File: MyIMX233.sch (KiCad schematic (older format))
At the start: 71 parts, among them IC1 iMX233, IC2 DDR_SDRAM_MT46_x16, J1 USB_A, J2 Micro_SD_Card, P1 P4v2, P2 1v2, P3 VDDA1v8, P4 2v5, P5 3v3, SW1 SWITCH_PUSHBUTTON, Y1 24Mhz

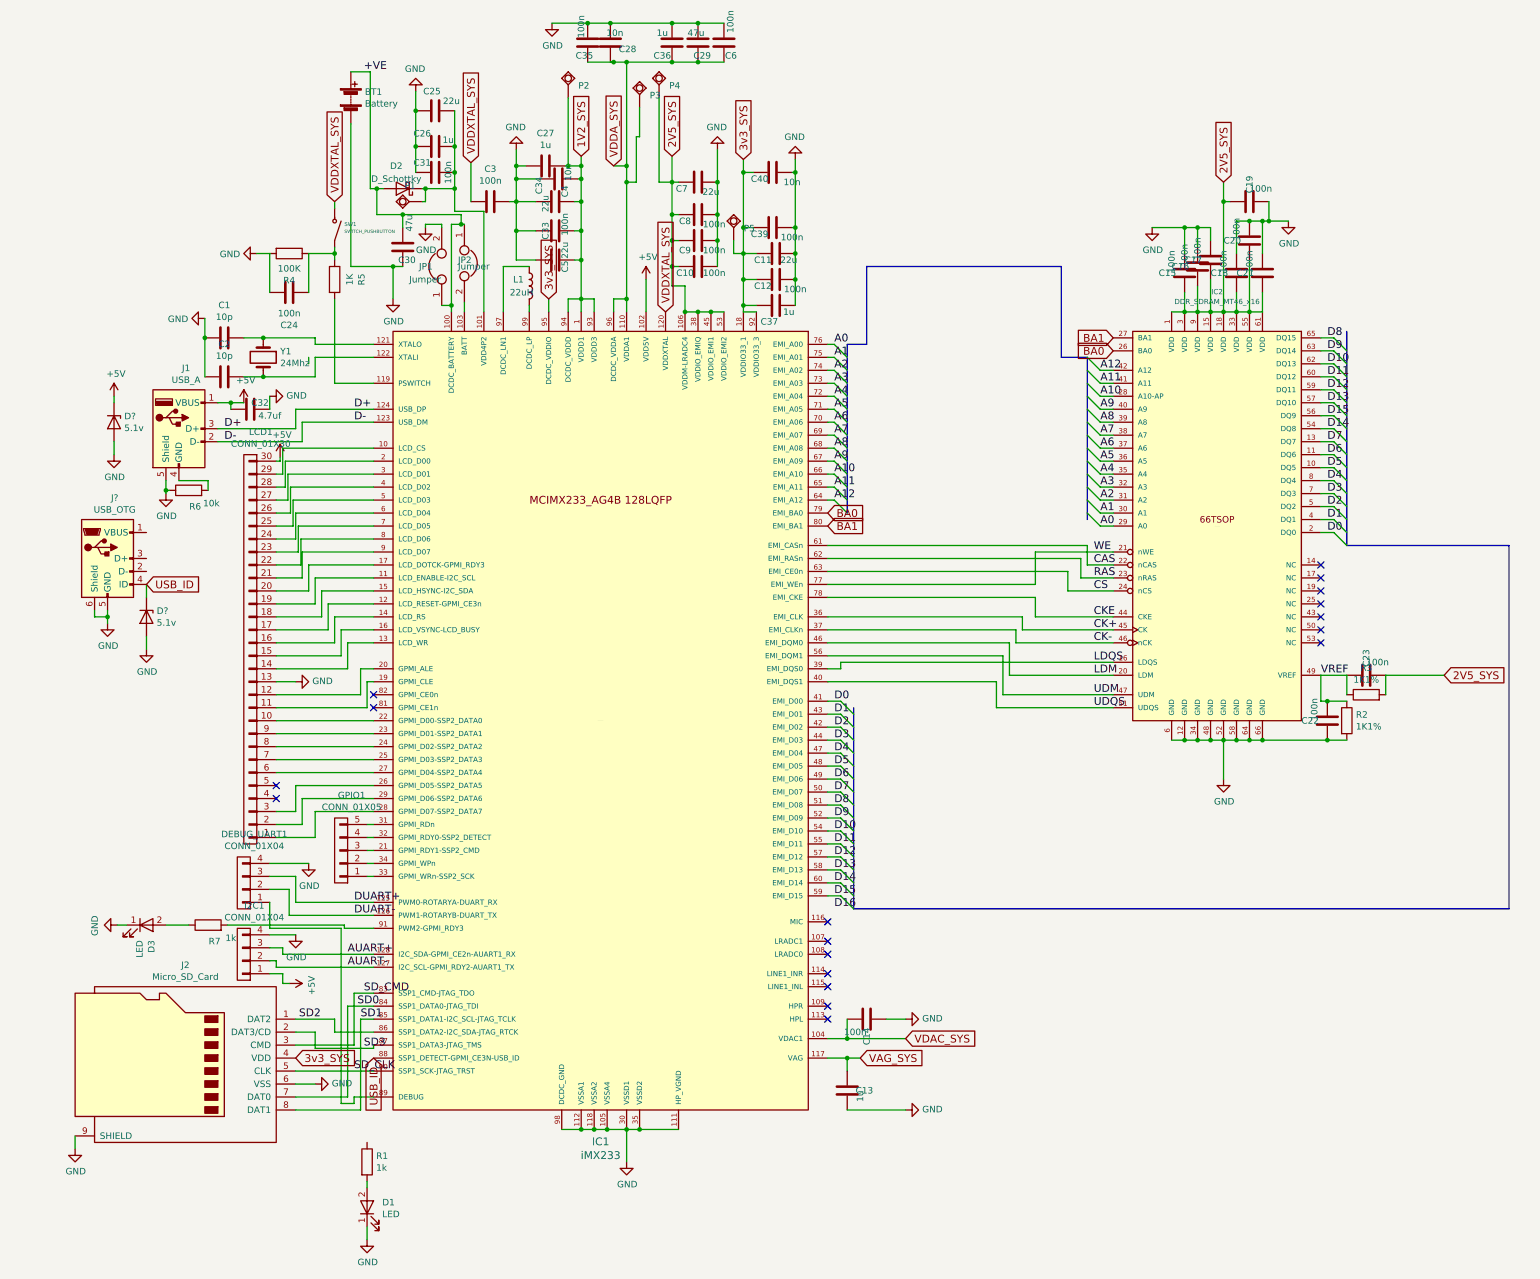
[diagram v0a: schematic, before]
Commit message: new uSD card connector added
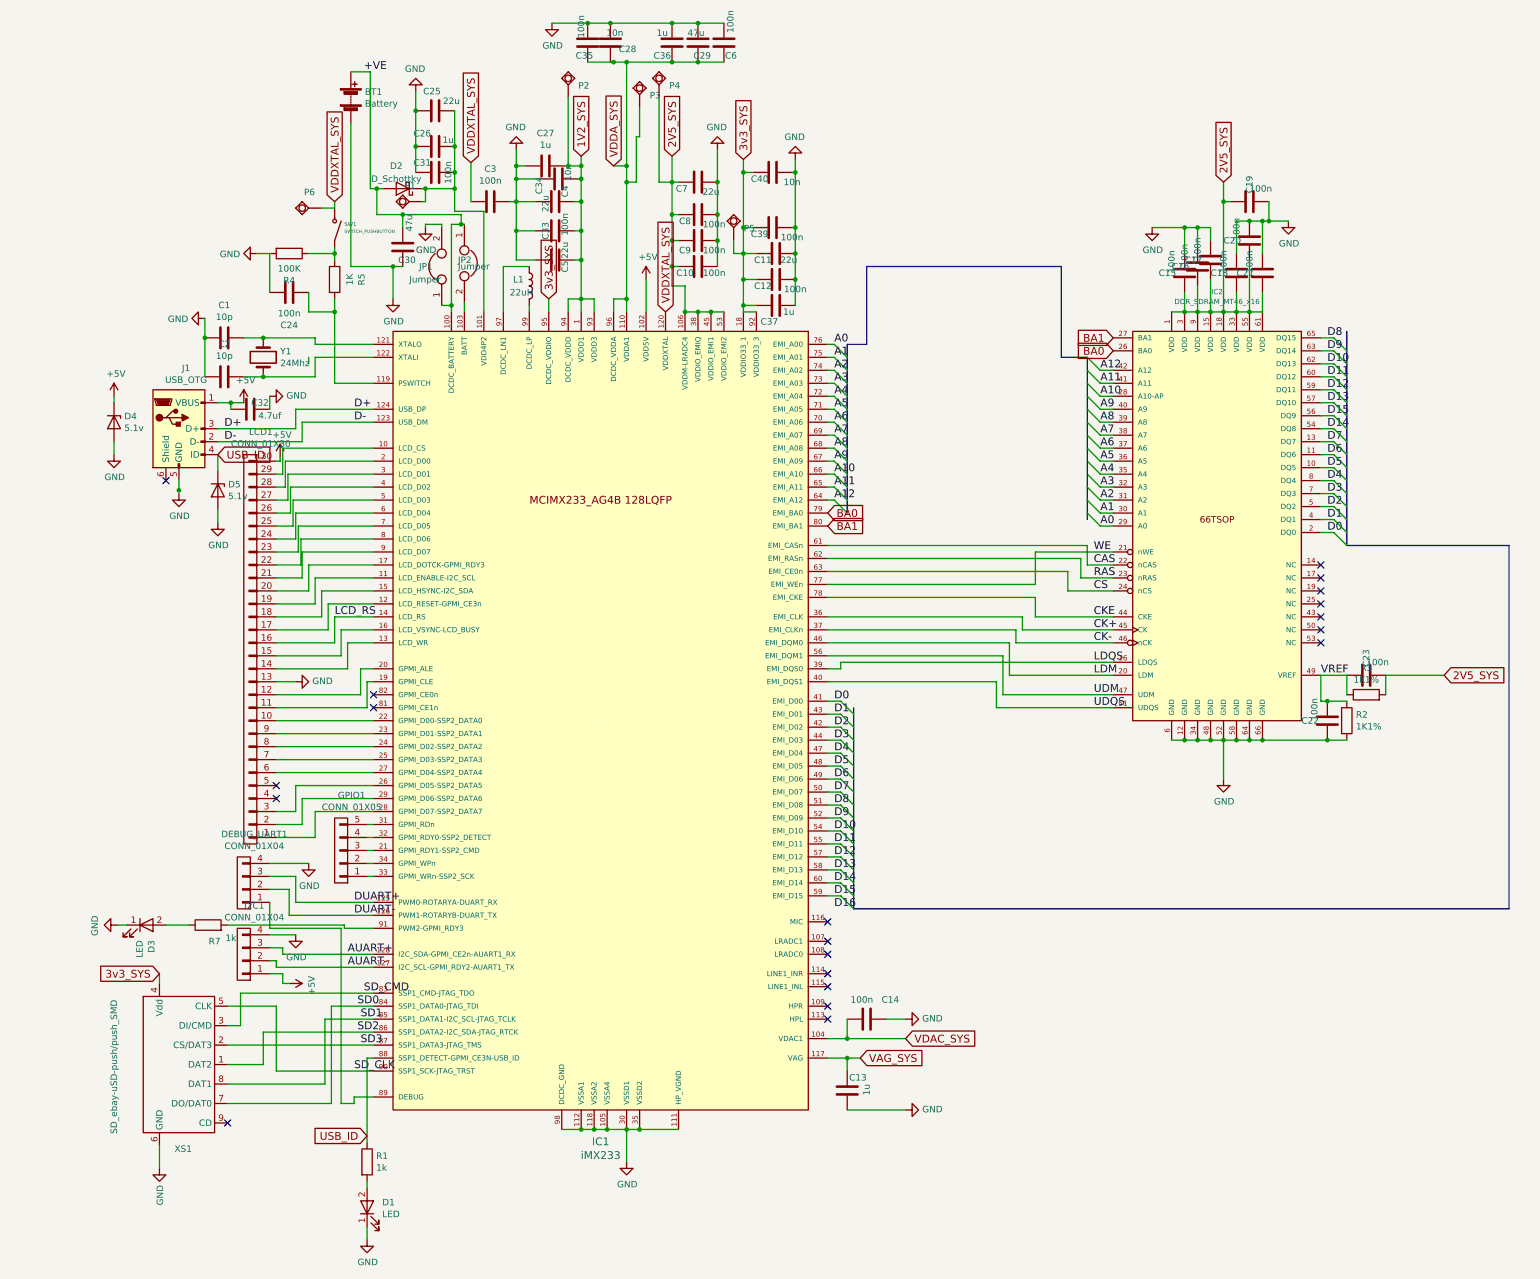
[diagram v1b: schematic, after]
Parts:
- removed J1: USB_A, conn-fci:CONN-10118194-0001LF-FCI, symbol USB_A
- removed J2: Micro_SD_Card, mylib:microSD_Card_Receptacle_Hirose_DM3AT-SF-PEJM5, symbol Micro_SD_Card
- removed J?: USB_OTG, symbol USB_OTG
- removed R6: 10k, Resistors_SMD:R_0603_HandSoldering, symbol R
- added J1: USB_OTG, mylib:CONN-10118194-0001LF-FCI, symbol USB_OTG
- added P6: P4v2, iMX233-OLinuXino-NANO_Rev_BEagle:GOGO_TESTPAD2, symbol GOGO_TESTPAD
- added XS1: SD_ebay-uSD-push/push_SMD, mylib:uSDcard, symbol SD_ebay-uSD-push/push_SMD
- D4, D5: renamed from D?; footprint (none) -> Diodes_SMD:D_SOD-323_HandSoldering
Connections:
- net +5V: now also J1.1 (VBUS)
- net 3v3_SYS: now also XS1.4 (Vdd)
- net D+: now also J1.3 (D+)
- net D-: now also J1.2 (D-)
- net GND: now also XS1.6 (GND)
- net SD0: now also XS1.7 (DO/DAT0)
- net SD1: now also XS1.8 (DAT1)
- net SD2: now also XS1.1 (DAT2)
- net SD3: now also XS1.2 (CS/DAT3)
- net SD_CLK: now also XS1.5 (CLK)
- net SD_CMD: now also XS1.3 (DI/CMD)
- net USB_ID: now also R1.1, J1.4 (ID)
- net VDDXTAL_SYS: now also P6.P$1 (PP)
- net at IC1.119 (PSWITCH), R5.2: now also C24.2
- net LCD_RS: now reaches IC1.14 (LCD_RS), LCD1.16 (P16)
- net at R4.1, R5.1, SW1.2 (B): no longer C24.2
- no-connect marks 18 -> 20
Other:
- moved on the sheet: D5

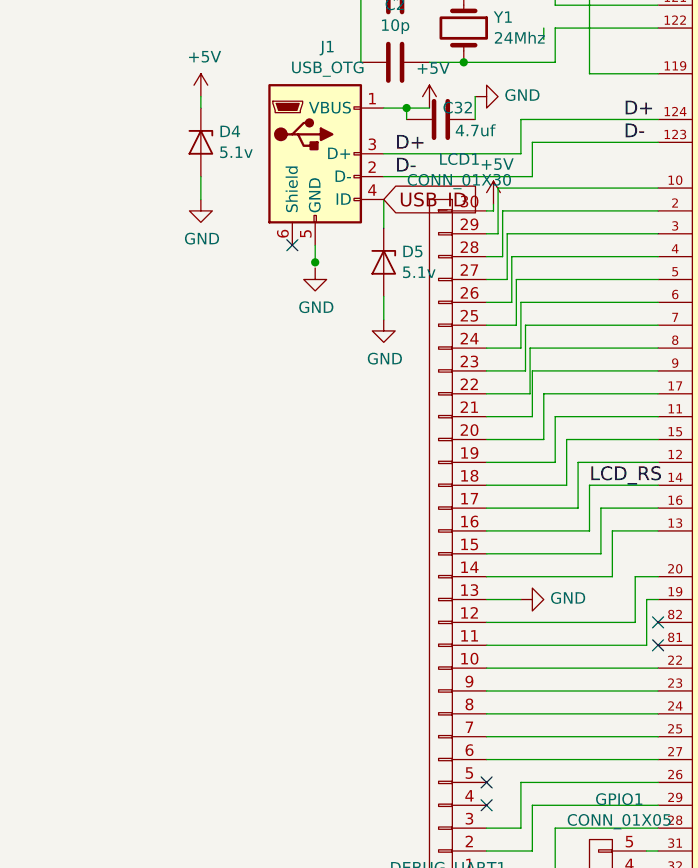
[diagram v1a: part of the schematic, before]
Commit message: usb footprint updated
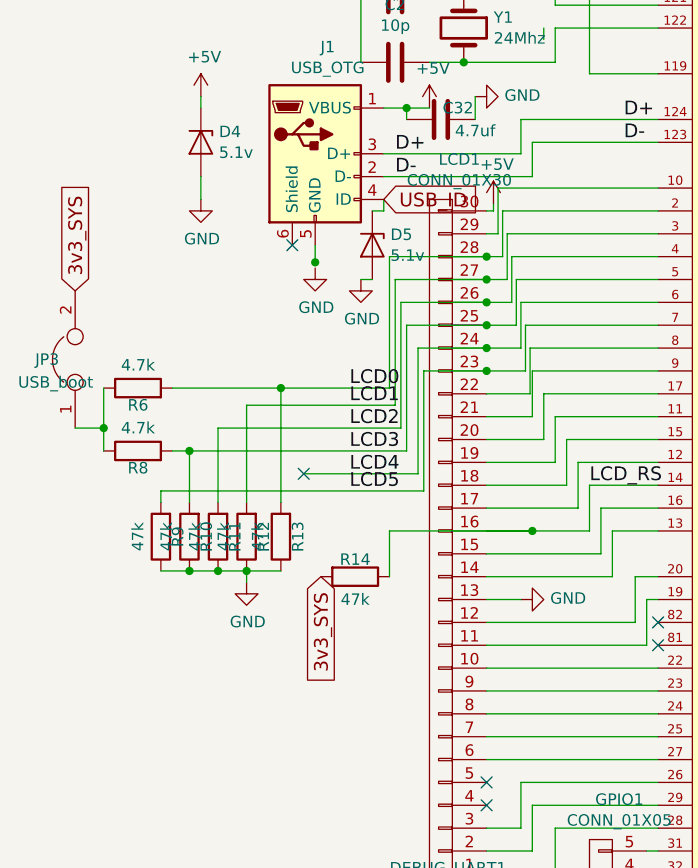
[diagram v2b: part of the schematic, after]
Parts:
- added JP3: USB_boot, Pin_Headers:Pin_Header_Straight_1x02_Pitch2.54mm, symbol Jumper
- added R10, R11, R12, R13, R14, R9: 47k, Resistors_SMD:R_0603_HandSoldering, symbol R
- added R6, R8: 4.7k, Resistors_SMD:R_0603_HandSoldering, symbol R
- J1: footprint mylib:CONN-10118194-0001LF-FCI -> mylib:USB_Micro-B_MOLEX_105017-0001
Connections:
- net 3v3_SYS: now also JP3.2, R14.2
- net GND: now also R10.1, R11.1, R12.1, R13.1, R9.1
- net LCD_RS: now also R14.1
- net LCD0: now reaches IC1.2 (LCD_D00), LCD1.28 (P28)
- net LCD0: now also R13.2, R6.2
- net LCD1: now reaches IC1.3 (LCD_D01), LCD1.27 (P27)
- net LCD1: now also R12.2
- net LCD2: now reaches IC1.4 (LCD_D02), LCD1.26 (P26)
- net LCD2: now also R11.2
- net LCD3: now reaches IC1.5 (LCD_D03), LCD1.25 (P25)
- net LCD3: now also R10.2, R8.2
- net LCD4: now reaches IC1.6 (LCD_D04), LCD1.24 (P24)
- net LCD5: now reaches IC1.7 (LCD_D05), LCD1.23 (P23)
- net LCD5: now also R9.2
- new net: JP3.1, R6.1, R8.1
- no-connect marks 20 -> 21
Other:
- moved on the sheet: D5
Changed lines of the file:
@@
 	2690 4500 3250 4500
 Wire Wire Line
-	2500 4600 2670 4600
+	2225 4600 2670 4600
 Wire Wire Line
 	2670 4600 2670 4400
@@
 	2670 4400 3250 4400
 Wire Wire Line
-	2500 4500 2650 4500
-Wire Wire Line
 	2650 4500 2650 4300
 Wire Wire Line
 	2650 4300 3250 4300
 Wire Wire Line
-	2500 4400 2630 4400
+	2150 4400 2630 4400
 Wire Wire Line
 	2630 4400 2630 4200
@@
 	2630 4200 3250 4200
 Wire Wire Line
-	2500 4300 2610 4300
+	2125 4300 2610 4300
 Wire Wire Line
 	2610 4300 2610 4100
@@
 	2610 4100 3250 4100
 Wire Wire Line
-	2500 4200 2590 4200
+	2100 4200 2590 4200
 Wire Wire Line
 	2590 4200 2590 4000
@@
 	2590 4000 3250 4000
 Wire Wire Line
-	2500 4100 2570 4100
+	2075 4100 2570 4100
 Wire Wire Line
 	2570 4100 2570 3900
@@
 L D_Zener D5
 U 1 1 598BC40A
-P 2050 4125
-F 0 "D5" V 2004 4204 50  0000 L CNN
-F 1 "5.1v" V 2095 4204 50  0000 L CNN
-F 2 "Diodes_SMD:D_SOD-323_HandSoldering" H 2050 4125 50  0001 C CNN
-F 3 "" H 2050 4125 50  0001 C CNN
-	1    2050 4125
+P 2000 4050
+F 0 "D5" V 1954 4129 50  0000 L CNN
+F 1 "5.1v" V 2045 4129 50  0000 L CNN
+F 2 "Diodes_SMD:D_SOD-323_HandSoldering" H 2000 4050 50  0001 C CNN
+F 3 "" H 2000 4050 50  0001 C CNN
+	1    2000 4050
 	0    1    1    0
 $EndComp
@@
 L GND #PWR030
 U 1 1 598BC5E8
-P 2050 4375
-F 0 "#PWR030" H 2050 4125 50  0001 C CNN
-F 1 "GND" H 2055 4202 50  0000 C CNN
-F 2 "" H 2050 4375 50  0001 C CNN
-F 3 "" H 2050 4375 50  0001 C CNN
-	1    2050 4375
+P 1950 4200
+F 0 "#PWR030" H 1950 3950 50  0001 C CNN
+F 1 "GND" H 1955 4027 50  0000 C CNN
+F 2 "" H 1950 4200 50  0001 C CNN
+F 3 "" H 1950 4200 50  0001 C CNN
+	1    1950 4200
 	1    0    0    -1
 $EndComp
@@
 F 0 "J1" H 1805 4117 50  0000 C CNN
 F 1 "USB_OTG" H 1805 4026 50  0000 C CNN
-F 2 "mylib:CONN-10118194-0001LF-FCI" H 1900 3600 50  0001 C CNN
+F 2 "mylib:USB_Micro-B_MOLEX_105017-0001" H 1900 3600 50  0001 C CNN
 F 3 "" H 1900 3600 50  0001 C CNN
 	1    1750 3650
@@
 $EndComp
 Wire Wire Line
-	2050 3975 2050 3850
-Wire Wire Line
 	1750 4125 1750 4050
 Connection ~ 1750 4125
-Wire Wire Line
-	2050 4275 2050 4375
 NoConn ~ 1650 4050
+$Comp
+L R R14
+U 1 1 5992DA70
+P 1925 5500
+F 0 "R14" V 1850 5500 50  0000 C CNN
+F 1 "47k" V 2025 5500 50  0000 C CNN
+F 2 "Resistors_SMD:R_0603_HandSoldering" V 1855 5500 50  0001 C CNN
+F 3 "" H 1925 5500 50  0001 C CNN
+	1    1925 5500
+	0    1    1    0
+$EndComp
+Connection ~ 2700 5300
+Text GLabel 700  4250 1    60   Input ~ 0
+3v3_SYS
+Connection ~ 2500 4100
+Connection ~ 2500 4200
+Connection ~ 2500 4300
+Connection ~ 2500 4400
+Wire Wire Line
+	1700 5050 2200 5050
+Connection ~ 2500 4500
+Connection ~ 2500 4600
+Wire Wire Line
+	2050 3900 2050 3850
+Wire Wire Line
+	1950 4200 2000 4200
+Wire Wire Line
+	2000 3900 2050 3900
+Wire Wire Line
+	2075 4675 2075 4100
+Wire Wire Line
+	1125 4675 2075 4675
+Wire Wire Line
+	2100 4750 2100 4200
+Wire Wire Line
+	2125 4850 2125 4300
+Wire Wire Line
+	2200 4500 2650 4500
+Wire Wire Line
+	2200 5050 2200 4500
+Wire Wire Line
+	2150 4950 2150 4400
+Wire Wire Line
+	1125 4950 2150 4950
+Wire Wire Line
+	2225 5125 2225 4600
+Wire Wire Line
+	1075 5125 2225 5125
+Text Label 1900 5125 0    60   ~ 0
+LCD5
+Text Label 1900 5050 0    60   ~ 0
+LCD4
+Text Label 1900 4950 0    60   ~ 0
+LCD3
+Text Label 1900 4850 0    60   ~ 0
+LCD2
+Text Label 1900 4750 0    60   ~ 0
+LCD1
+Text Label 1900 4675 0    60   ~ 0
+LCD0
+$Comp
+L R R13
+U 1 1 59940018
+P 1600 5325
+F 0 "R13" V 1525 5325 50  0000 C CNN
+F 1 "47k" V 1700 5325 50  0000 C CNN
+F 2 "Resistors_SMD:R_0603_HandSoldering" V 1530 5325 50  0001 C CNN
+F 3 "" H 1600 5325 50  0001 C CNN
+	1    1600 5325
+	-1   0    0    1
+$EndComp
+$Comp
+L GND #PWR031
+U 1 1 599401F2
+P 1450 5525
+F 0 "#PWR031" H 1450 5275 50  0001 C CNN
+F 1 "GND" H 1455 5352 50  0000 C CNN
+F 2 "" H 1450 5525 50  0001 C CNN
+F 3 "" H 1450 5525 50  0001 C CNN
+	1    1450 5525
+	1    0    0    -1
+$EndComp
+$Comp
+L R R12
+U 1 1 59941454
+P 1450 5325
+F 0 "R12" V 1375 5325 50  0000 C CNN
+F 1 "47k" V 1550 5325 50  0000 C CNN
+F 2 "Resistors_SMD:R_0603_HandSoldering" V 1380 5325 50  0001 C CNN
+F 3 "" H 1450 5325 50  0001 C CNN
+	1    1450 5325
+	-1   0    0    1
+$EndComp
+$Comp
+L R R11
+U 1 1 5994150A
+P 1325 5325
+F 0 "R11" V 1250 5325 50  0000 C CNN
+F 1 "47k" V 1425 5325 50  0000 C CNN
+F 2 "Resistors_SMD:R_0603_HandSoldering" V 1255 5325 50  0001 C CNN
+F 3 "" H 1325 5325 50  0001 C CNN
+	1    1325 5325
+	-1   0    0    1
+$EndComp
+$Comp
+L R R10
+U 1 1 599415B8
+P 1200 5325
+F 0 "R10" V 1125 5325 50  0000 C CNN
+F 1 "47k" V 1300 5325 50  0000 C CNN
+F 2 "Resistors_SMD:R_0603_HandSoldering" V 1130 5325 50  0001 C CNN
+F 3 "" H 1200 5325 50  0001 C CNN
+	1    1200 5325
+	-1   0    0    1
+$EndComp
+NoConn ~ 1700 5050
+Wire Wire Line
+	1600 5175 1600 4675
+Connection ~ 1600 4675
+Wire Wire Line
+	1450 5175 1450 4750
+Wire Wire Line
+	1325 5175 1325 4850
+Wire Wire Line
+	1325 4850 2125 4850
+Wire Wire Line
+	1200 5175 1200 4950
+Connection ~ 1200 4950
+$Comp
+L R R9
+U 1 1 59942CD2
+P 1075 5325
+F 0 "R9" V 1000 5325 50  0000 C CNN
+F 1 "47k" V 1175 5325 50  0000 C CNN
+F 2 "Resistors_SMD:R_0603_HandSoldering" V 1005 5325 50  0001 C CNN
+F 3 "" H 1075 5325 50  0001 C CNN
+	1    1075 5325
+	-1   0    0    1
+$EndComp
+Wire Wire Line
+	1075 5175 1075 5125
+Wire Wire Line
+	1075 5475 1600 5475
+Connection ~ 1200 5475
+Connection ~ 1325 5475
+Connection ~ 1450 5475
+Wire Wire Line
+	1450 5525 1450 5475
+Wire Wire Line
+	2075 5500 2075 5300
+Wire Wire Line
+	2075 5300 2700 5300
+$Comp
+L R R6
+U 1 1 599451CF
+P 975 4675
+F 0 "R6" V 900 4675 50  0000 C CNN
+F 1 "4.7k" V 1075 4675 50  0000 C CNN
+F 2 "Resistors_SMD:R_0603_HandSoldering" V 905 4675 50  0001 C CNN
+F 3 "" H 975 4675 50  0001 C CNN
+	1    975  4675
+	0    -1   -1   0
+$EndComp
+$Comp
+L R R8
+U 1 1 5994533A
+P 975 4950
+F 0 "R8" V 900 4950 50  0000 C CNN
+F 1 "4.7k" V 1075 4950 50  0000 C CNN
+F 2 "Resistors_SMD:R_0603_HandSoldering" V 905 4950 50  0001 C CNN
+F 3 "" H 975 4950 50  0001 C CNN
+	1    975  4950
+	0    -1   -1   0
+$EndComp
+Wire Wire Line
+	825  4950 825  4675
+Text GLabel 1775 5500 3    60   Input ~ 0
+3v3_SYS
+Wire Wire Line
+	1450 4750 2100 4750
+$Comp
+L Jumper JP3
+U 1 1 59949205
+P 700 4550
+F 0 "JP3" V 700 4725 50  0000 R CNN
+F 1 "USB_boot" V 600 4800 50  0000 R CNN
+F 2 "Pin_Headers:Pin_Header_Straight_1x02_Pitch2.54mm" H 700 4550 50  0001 C CNN
+F 3 "" H 700 4550 50  0001 C CNN
+	1    700  4550
+	0    -1   -1   0
+$EndComp
+Wire Wire Line
+	700  4850 825  4850
+Connection ~ 825  4850
 $EndSCHEMATC
